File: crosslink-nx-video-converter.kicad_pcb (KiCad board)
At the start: 8 copper layers, 105.7 x 68 mm, 282 parts, among them J1 DC_SOCKET, J2 031-70526-21, J3 031-70526-21, J4 WE_68715014522_ONE-SIDE, J5 FTSH-105-01-F-DV-K, J6 WE_68715014522_ONE-SIDE, J7 2X05, J8 61300411121, Q1 2N7002, Q2 AO3401A, Q3 AO3401A, Q4 2N7002, Q5 AO3401A, Q6 2N7002, SW1 SW_DIP_x06, U1 MP20073, U10 AP7330-W5-7, U11 LIFCL-40-9BG256C, U12 MT41K128M16JT-125_K, U15 GS2971A, U16 GS2988, U17 SC18IS602BIPW, U18 W25Q32JVSSIQ, U2 LM339, U3 LM339, U5 AP62301WU-7, U6 AP62301WU-7, U7 AP62301WU-7, U8 AP7330-W5-7, U9 AP7330-W5-7, Y1 ABM7_27.000MH_D2Y_T, Y2 OSC40M-3.3_S5

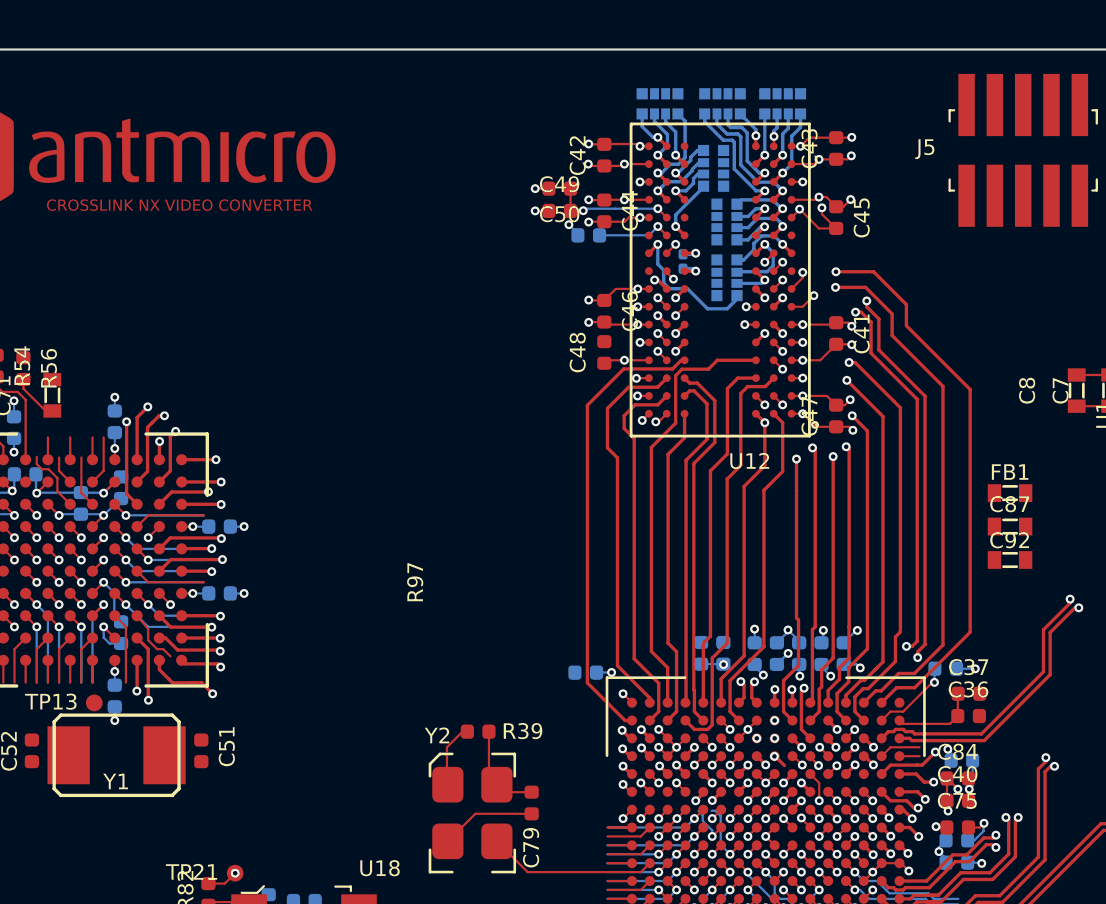
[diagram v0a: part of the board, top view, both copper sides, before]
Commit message: Rerouted some DDR3 signals
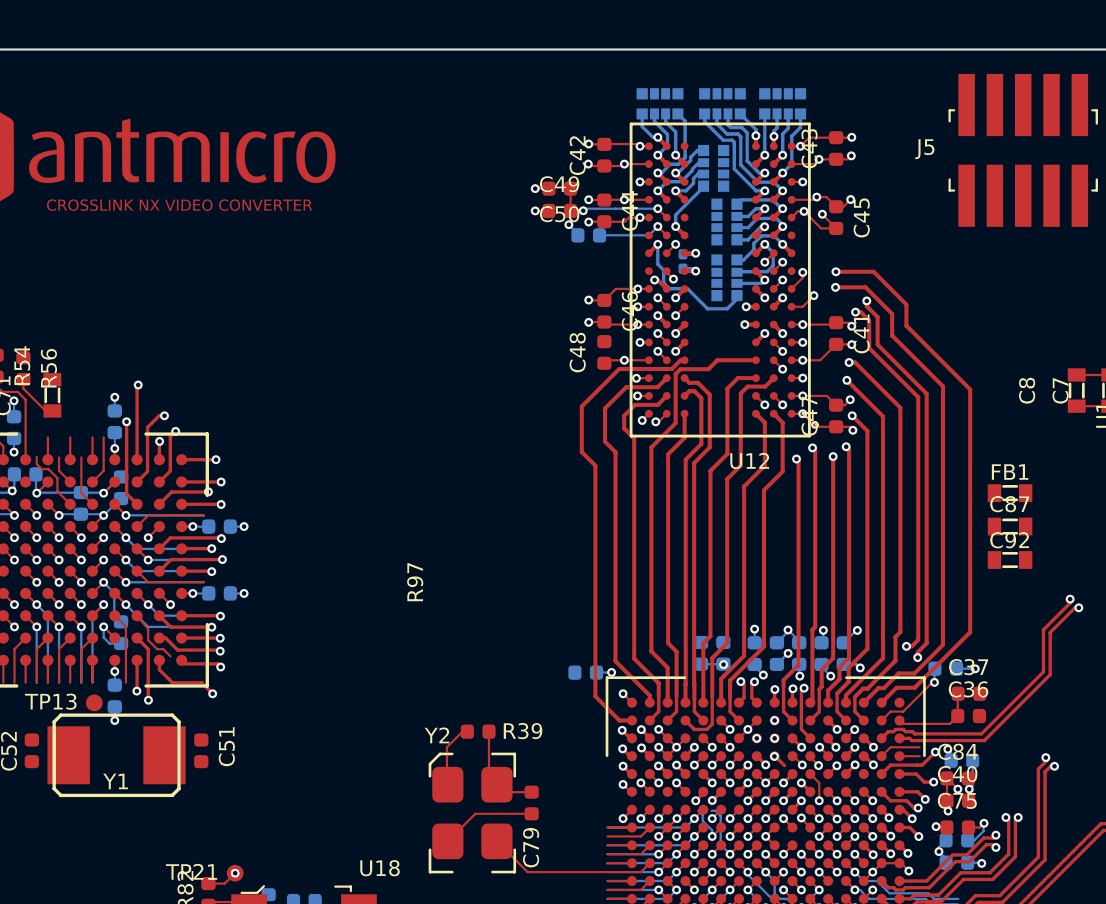
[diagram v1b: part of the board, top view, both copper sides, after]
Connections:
- U11 pad L11: /DDR3/DDR3_A13 -> /DDR3/DDR3_A2
- U11 pad L9: /DDR3/~{DDR3_RESET} -> /DDR3/DDR3_A5
- U11 pad N8: /DDR3/DDR3_A2 -> /DDR3/DDR3_A13
- U11 pad N9: /DDR3/DDR3_A5 -> /DDR3/~{DDR3_RESET}
- U11 pad P7: /DDR3/DDR3_A3 -> /DDR3/DDR3_A0
- U11 pad P8: /DDR3/DDR3_A0 -> /DDR3/DDR3_A3
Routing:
- net /DDR3/DDR3_A13: track 67.2 -> 48.8 mm
- net /DDR3/~{DDR3_RESET}: track 59.6 -> 47.1 mm
- net /DDR3/DDR3_A9: track 57.1 -> 49.2 mm
- net /SDI/SDI_PCLK: track 41.1 -> 47.5 mm
- net /DDR3/DDR3_A7: track 54.4 -> 48.3 mm
- net /DDR3/DDR3_A2: track 53.7 -> 48.7 mm
- net /DDR3/DDR3_A0: track 45.1 -> 47.6 mm
- net /DDR3/DDR3_A5: track 49.5 -> 47.6 mm
- net /DDR3/DDR3_BA2: track 41.8 -> 42.7 mm
- net /DDR3/DDR3_A3: track 46.2 -> 45.3 mm
- net /DDR3/DDR3_CKE: track 34.9 -> 34.3 mm
- net /DDR3/DDR3_DQ15: track 14.0 -> 13.9 mm, vias 1 -> 0

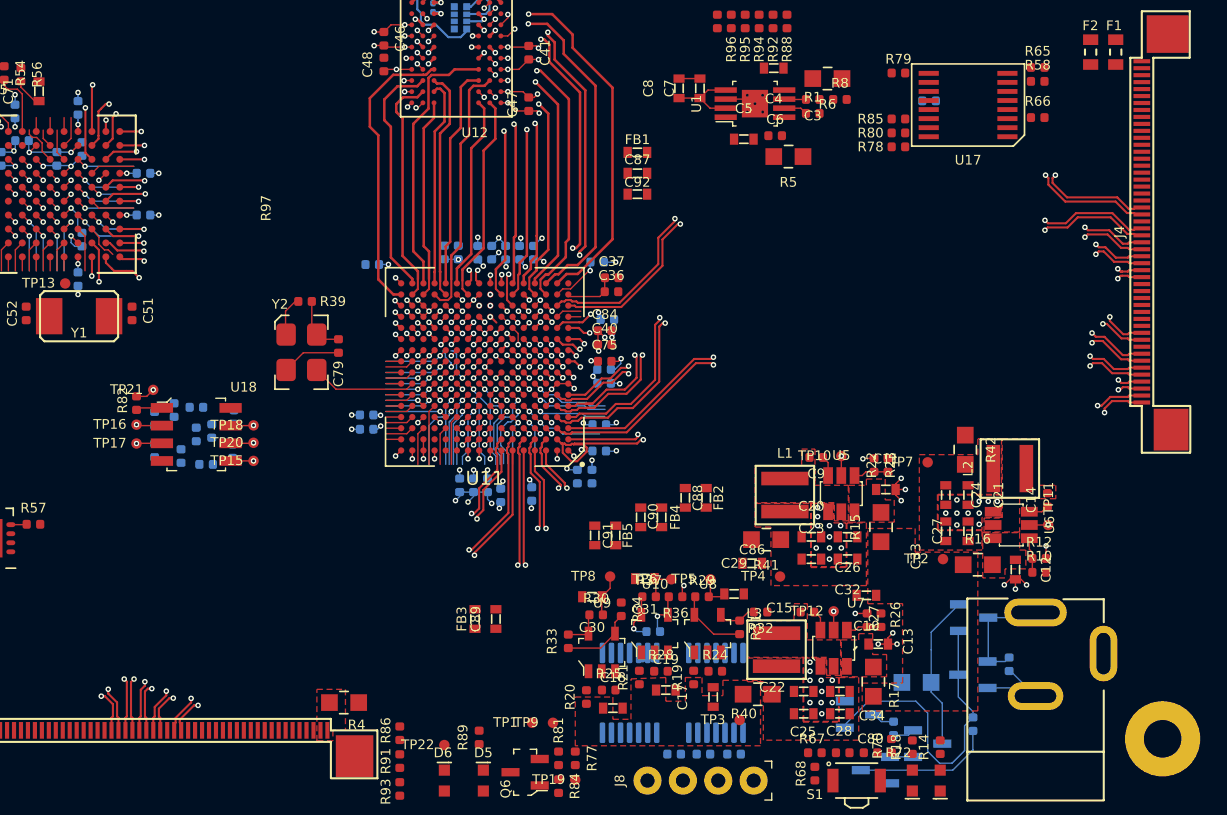
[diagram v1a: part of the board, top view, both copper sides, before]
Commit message: Fixed SDI top impedance
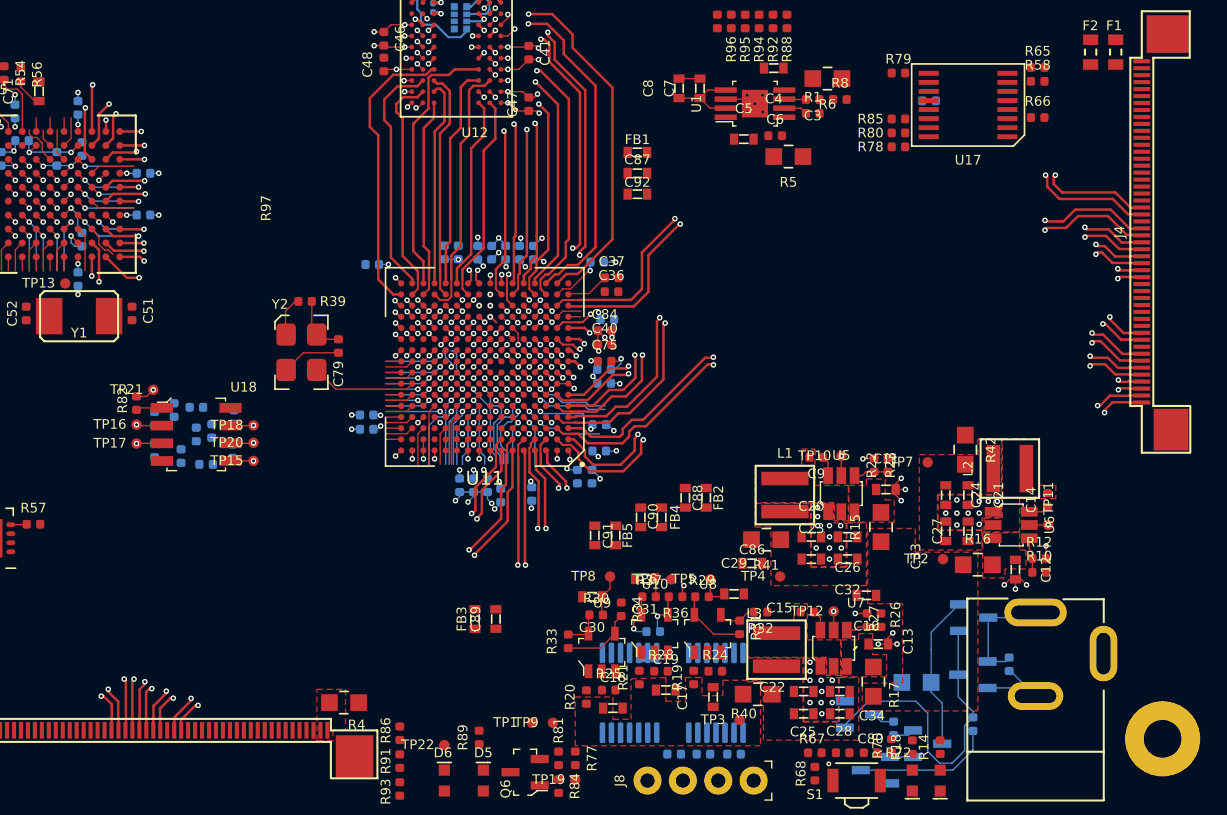
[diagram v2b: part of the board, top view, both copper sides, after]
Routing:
- net /Peripherals/MIPI0_D3_P: track 42.7 -> 44.9 mm
- net /Peripherals/MIPI0_D3_N: track 47.9 -> 45.9 mm
- net /Peripherals/MIPI1_D2_P: track 48.8 -> 48.0 mm
- net Vref: track 11.9 -> 11.1 mm
- net /Peripherals/MIPI0_D1_P: track 43.8 -> 44.4 mm
- net /Peripherals/MIPI0_D1_N: track 44.8 -> 45.4 mm
- net /Peripherals/MIPI1_D2_N: track 49.8 -> 49.2 mm
- net /Peripherals/MIPI1_D3_N: track 48.0 -> 47.5 mm
- net /Peripherals/MIPI0_D0_N: track 46.8 -> 46.3 mm
- net /Peripherals/MIPI0_D0_P: track 46.0 -> 45.5 mm

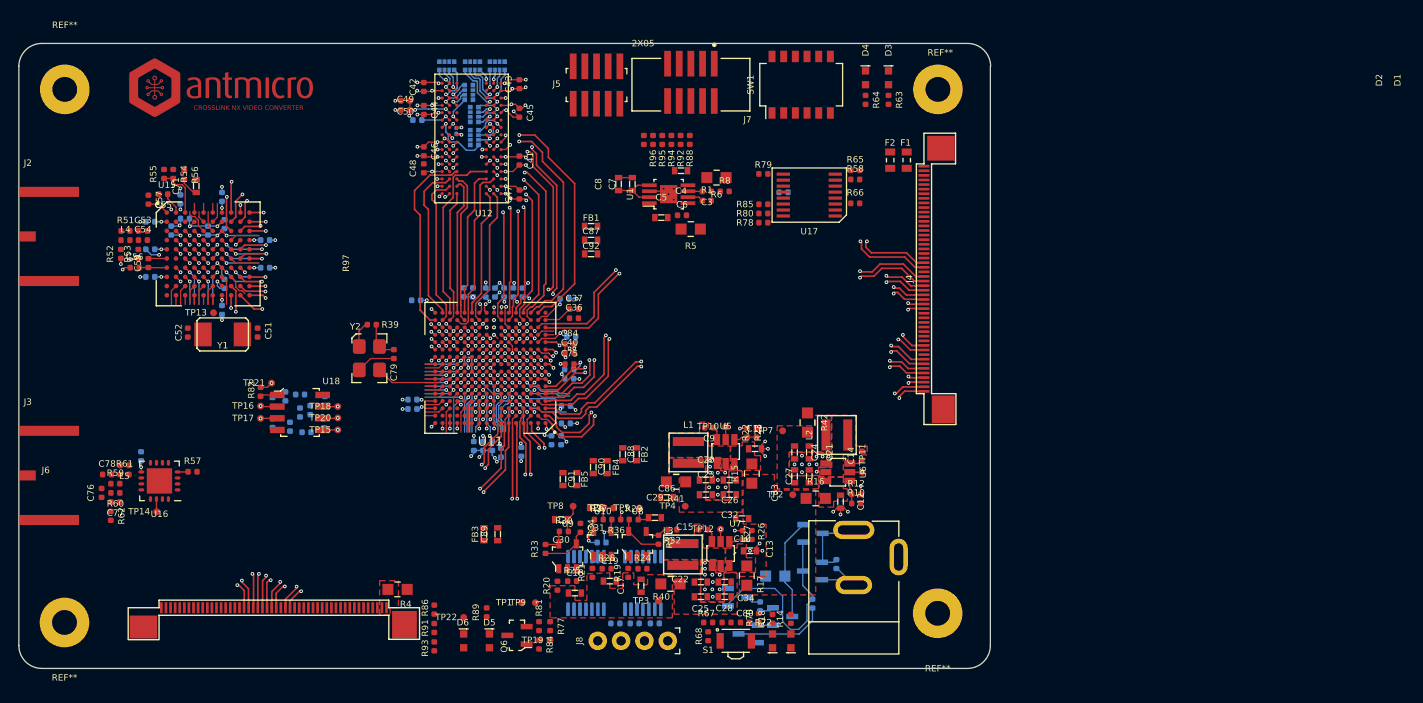
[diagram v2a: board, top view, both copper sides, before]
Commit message: Length matched most high speed interfaces
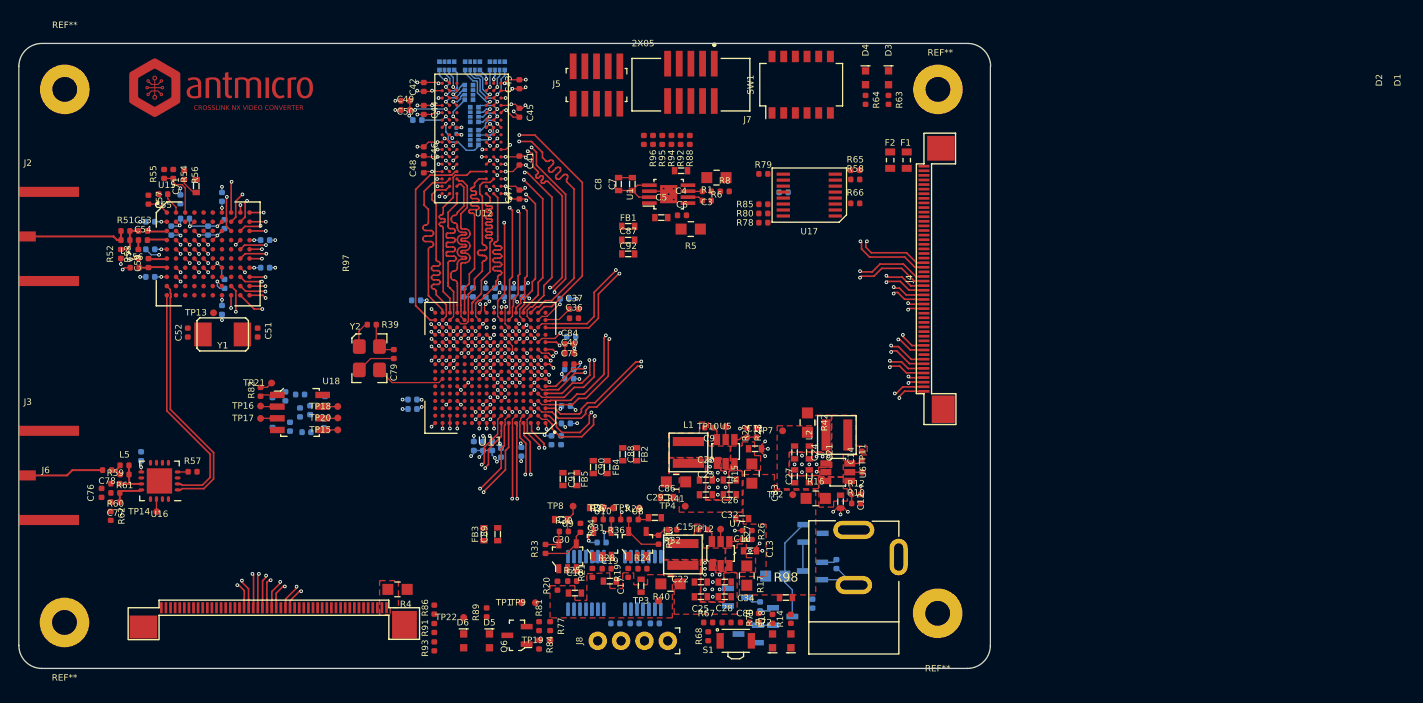
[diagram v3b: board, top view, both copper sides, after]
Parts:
- added R98: R_1k_0603, antmicro-footprints:0603-res, F.Cu at (158.5, 115.3)
- moved C87 4.04 mm to (141.3, 76.4)
- moved C92 4.04 mm to (141.3, 77.9)
- moved FB1 4.04 mm to (141.3, 74.9)
- moved C78 0.48 mm to (84.6, 101.4), turned to 180 degrees
- turned L4 to 180 degrees
- turned L5 to 0 degrees
- turned R61 to 180 degrees
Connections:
- net Net-(C54-Pad1) renamed /SDI/SDI_N2
- net Net-(C56-Pad2) renamed /SDI/AGC_N
- net Net-(C59-Pad2) renamed /SDI/AGC_P
- Q1 pad 1: ALT_5V -> Net-(Q1-Pad1)
- R7 pad 2: ALT_5V -> Net-(Q1-Pad1)
- R9 pad 1: Net-(Q1-Pad3) -> Net-(Q1-Pad1)
- R9 pad 2: Net-(Q3-Pad3) -> ALT_5V
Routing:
- net /SDI/SDI_D7: track 40.8 -> 77.0 mm
- net /SDI/SDO_P: track 0.00 -> 27.5 mm
- net /SDI/SDO_N: track 0.00 -> 25.7 mm
- net /SDI/SDI_D15: track 36.1 -> 57.3 mm
- net /DDR3/DDR3_CK_P: track 27.5 -> 48.2 mm
- net /DDR3/DDR3_CK_N: track 28.5 -> 48.2 mm
- net Net-(Q1-Pad3): track 22.6 -> 3.10 mm
- net /Peripherals/MIPI0_D2_N: track 43.6 -> 63.0 mm
- net /Peripherals/MIPI0_D2_P: track 42.6 -> 62.0 mm
- net /SDI/SDI_D13: track 37.9 -> 57.3 mm
- net /DDR3/DDR3_CKE: track 34.3 -> 53.4 mm
- net /DDR3/~{DDR3_CAS}: track 31.5 -> 50.5 mm
- net /DDR3/DDR3_ODT: track 31.8 -> 50.6 mm
- net /DDR3/DDR3_A10: track 31.6 -> 49.8 mm
- net /SDI/SDI_D16: track 40.0 -> 57.4 mm
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- removed copper zone on In6.Cu, net GND

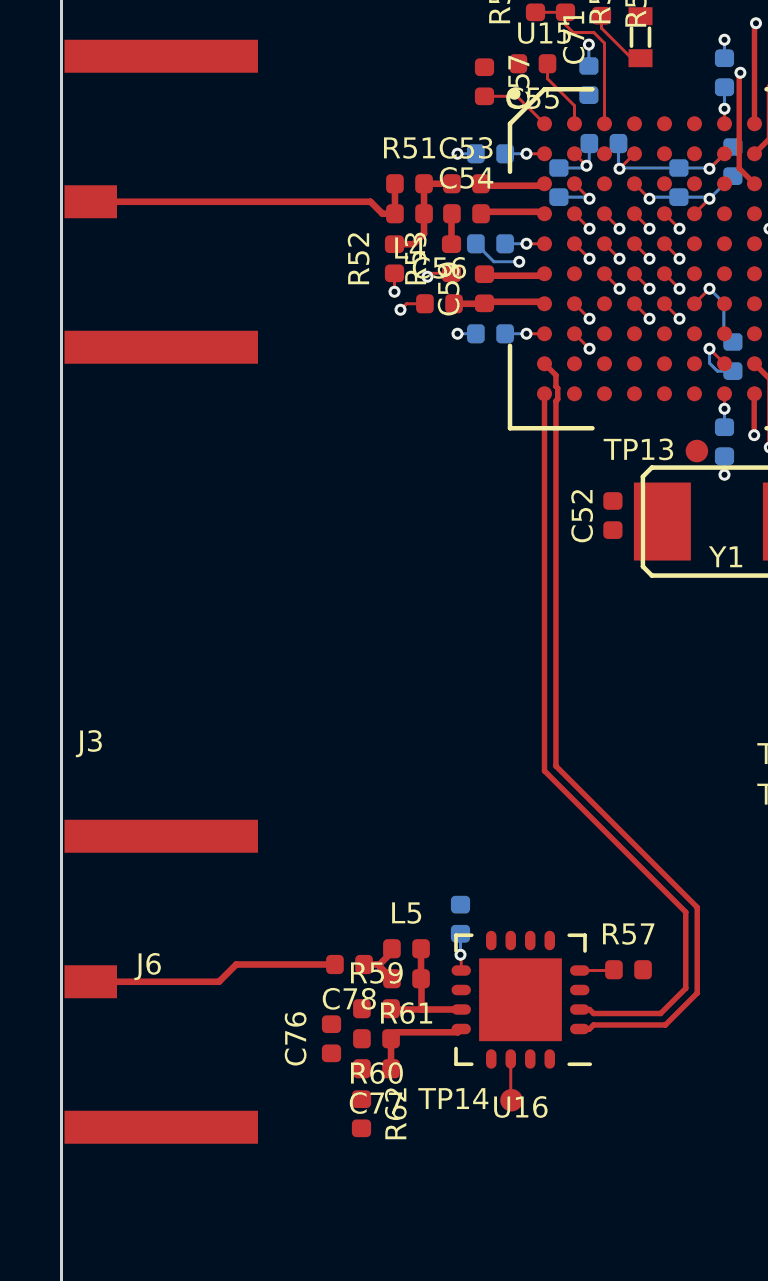
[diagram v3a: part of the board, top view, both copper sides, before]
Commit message: Small fixes to high speed signals
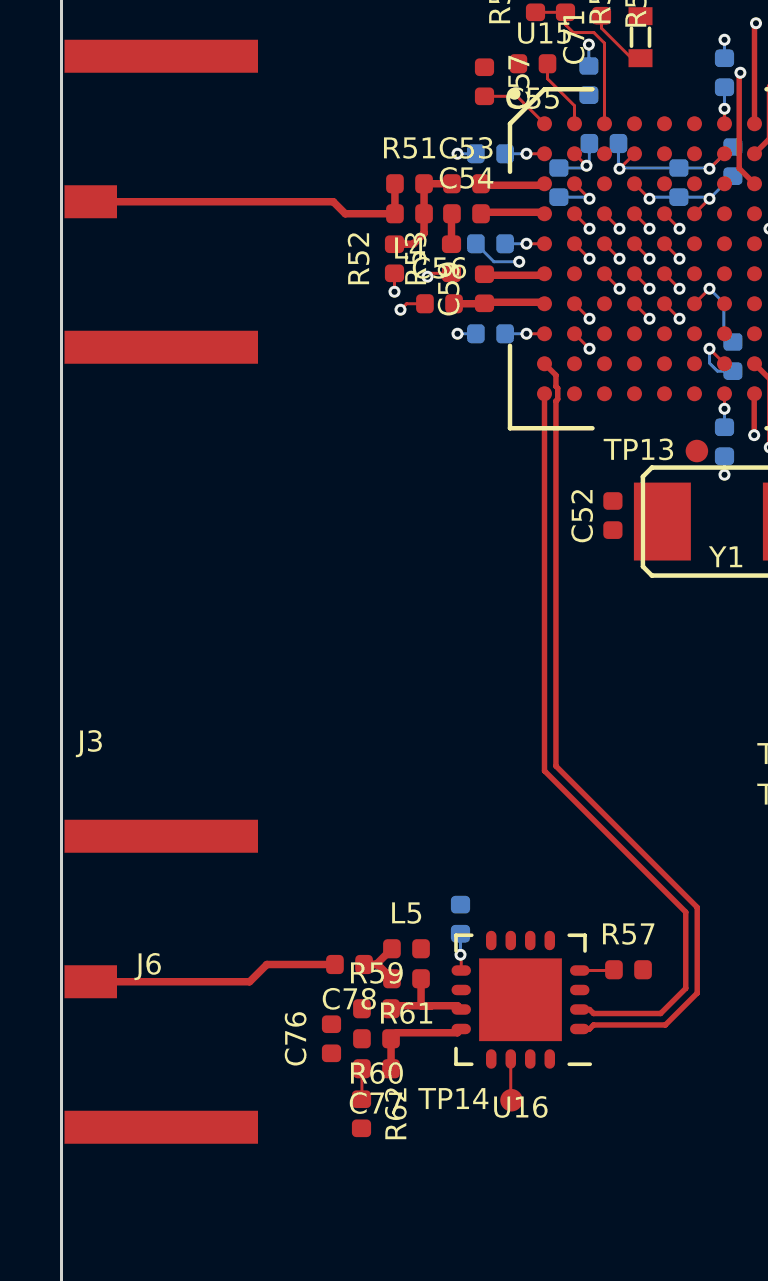
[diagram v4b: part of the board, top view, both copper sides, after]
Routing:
- net Net-(C77-Pad2): track 0.00 -> 1.02 mm
- net /SDI/SDI_OUT_N: track 4.74 -> 3.85 mm
- removed copper zone on In5.Cu, net +1V5
